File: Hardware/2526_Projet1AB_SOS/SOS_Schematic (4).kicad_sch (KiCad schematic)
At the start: 61 parts, among them J1 USB_C_Receptacle_USB2.0_16P, J2 Conn_ST_STDC14, SW1 SW_SPDT, SW2 SW_Push, SW3 SW_Push, SW4 SW_Push, SW5 SW_Push, U1 BU33SD5WG-TR, U2 USBLC6-2SC6, U3 STM32L476RGTx, Y1 20MHz

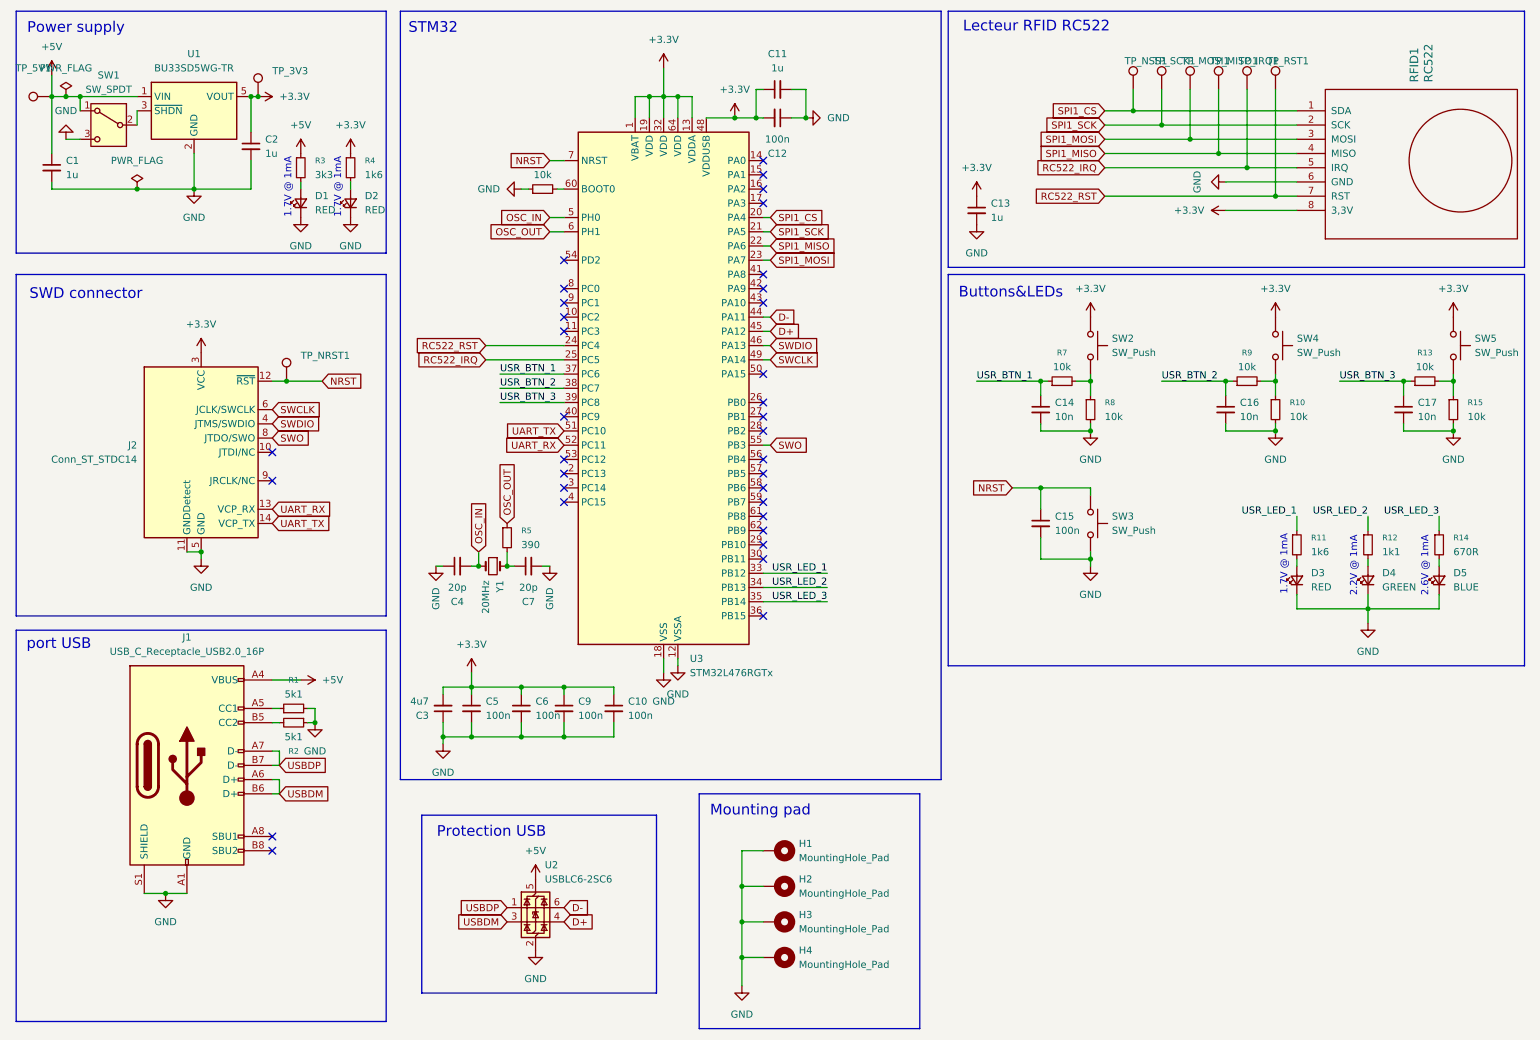
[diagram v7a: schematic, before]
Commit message: Routage Board (sauf port USB)
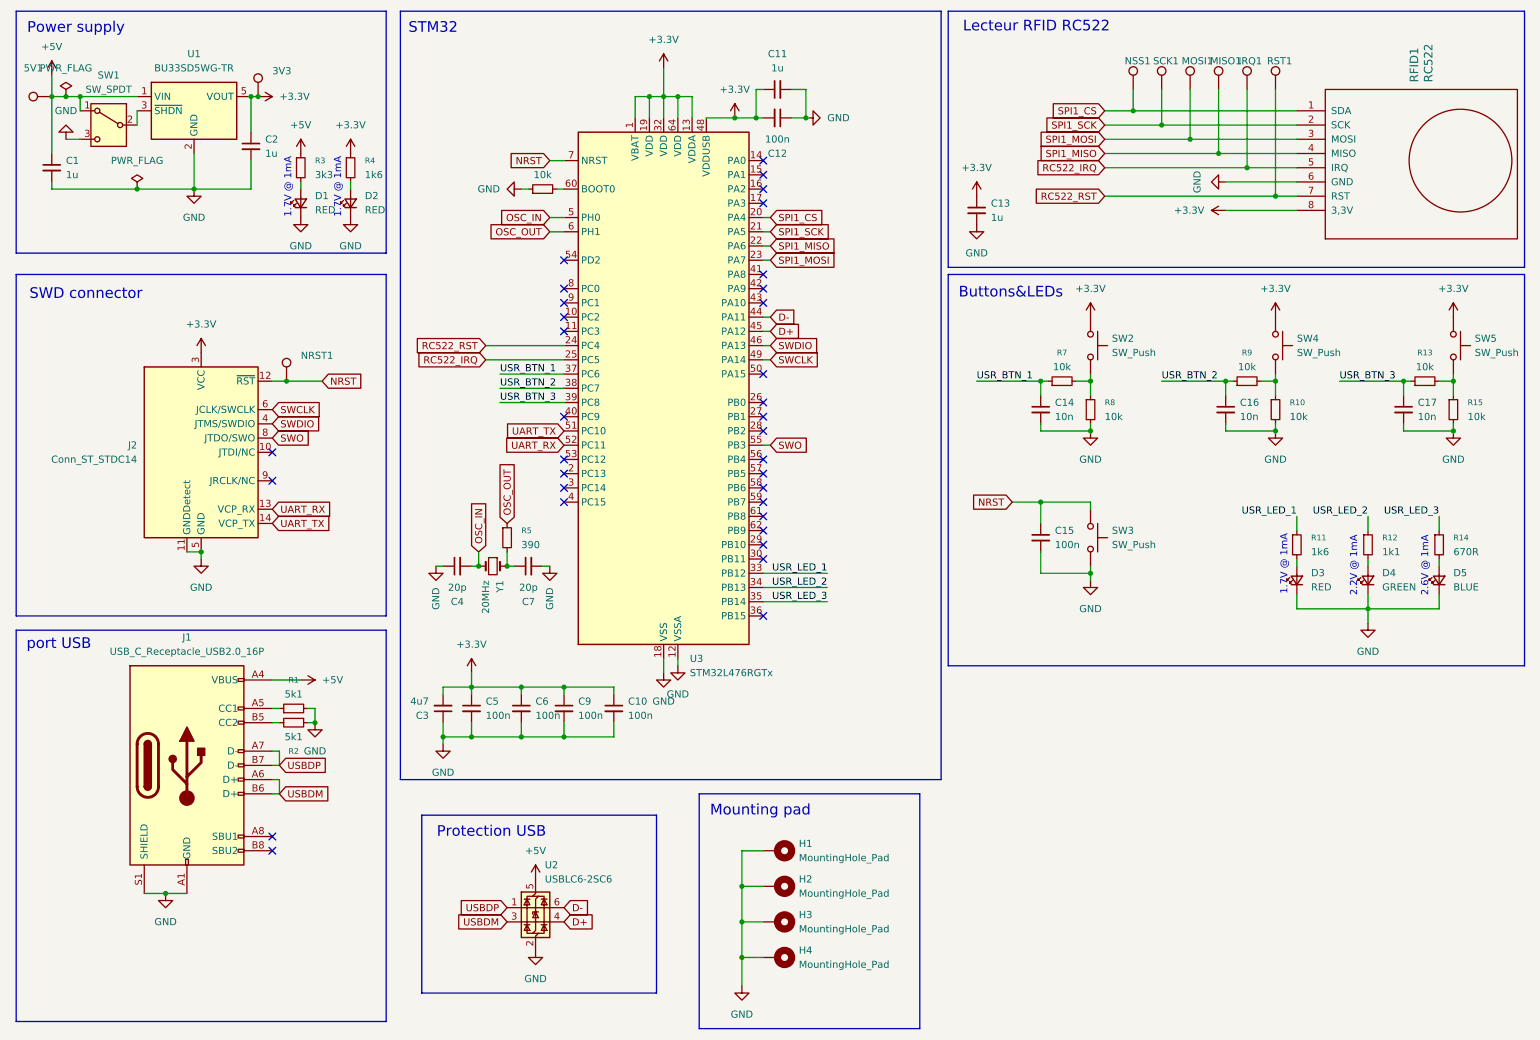
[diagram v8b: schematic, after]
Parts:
- renumbered TP_3V3 to 3V3, TP_5V1 to 5V1, TP_IRQ1 to IRQ1, TP_MISO1 to MISO1, TP_MOSI1 to MOSI1, TP_NRST1 to NRST1, TP_NSS1 to NSS1, TP_RST1 to RST1, TP_SCK1 to SCK1
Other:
- moved on the sheet: C15, SW3
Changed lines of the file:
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@@
 	)
 	(junction
-		(at 196.85 99.06)
+		(at 196.85 101.6)
 		(diameter 0)
 		(color 0 0 0 0)
@@
 	)
 	(junction
-		(at 205.74 111.76)
+		(at 205.74 114.3)
 		(diameter 0)
 		(color 0 0 0 0)
@@
 	(wire
 		(pts
-			(xy 191.77 99.06) (xy 196.85 99.06)
+			(xy 191.77 101.6) (xy 196.85 101.6)
 		)
 		(stroke
@@
 	(wire
 		(pts
-			(xy 196.85 99.06) (xy 196.85 102.87)
+			(xy 196.85 101.6) (xy 196.85 105.41)
 		)
 		(stroke
@@
 	(wire
 		(pts
-			(xy 205.74 111.76) (xy 205.74 113.03)
+			(xy 205.74 114.3) (xy 205.74 115.57)
 		)
 		(stroke
@@
 	(wire
 		(pts
-			(xy 196.85 99.06) (xy 205.74 99.06)
+			(xy 196.85 101.6) (xy 205.74 101.6)
 		)
 		(stroke
@@
 	(wire
 		(pts
-			(xy 196.85 111.76) (xy 205.74 111.76)
+			(xy 196.85 114.3) (xy 205.74 114.3)
 		)
 		(stroke
@@
 	(wire
 		(pts
-			(xy 205.74 99.06) (xy 205.74 100.33)
+			(xy 205.74 101.6) (xy 205.74 102.87)
 		)
 		(stroke
@@
 	(wire
 		(pts
-			(xy 205.74 110.49) (xy 205.74 111.76)
+			(xy 205.74 113.03) (xy 205.74 114.3)
 		)
 		(stroke
@@
 	(wire
 		(pts
-			(xy 196.85 107.95) (xy 196.85 111.76)
+			(xy 196.85 110.49) (xy 196.85 114.3)
 		)
 		(stroke
@@
 	(global_label "NRST"
 		(shape input)
-		(at 191.77 99.06 180)
+		(at 191.77 101.6 180)
 		(fields_autoplaced yes)
 		(effects
@@
 		)
 		(property "Intersheetrefs" "${INTERSHEET_REFS}"
-			(at 184.0072 99.06 0)
+			(at 184.0072 101.6 0)
 			(effects
 				(font
@@
 	(symbol
 		(lib_id "Device:C_Small")
-		(at 196.85 105.41 0)
+		(at 196.85 107.95 0)
 		(unit 1)
 		(exclude_from_sim no)
@@
 		(fields_autoplaced yes)
 		(property "Reference" "C15"
-			(at 199.39 104.1462 0)
+			(at 199.39 106.6862 0)
 			(effects
 				(font
@@
 		)
 		(property "Value" "100n"
-			(at 199.39 106.6862 0)
+			(at 199.39 109.2262 0)
 			(effects
 				(font
@@
 		)
 		(property "Footprint" "Capacitor_SMD:C_0603_1608Metric"
-			(at 196.85 105.41 0)
+			(at 196.85 107.95 0)
 			(effects
 				(font
@@
 		)
 		(property "Datasheet" "~"
-			(at 196.85 105.41 0)
+			(at 196.85 107.95 0)
 			(effects
 				(font
@@
 		)
 		(property "Description" "Unpolarized capacitor, small symbol"
-			(at 196.85 105.41 0)
+			(at 196.85 107.95 0)
 			(effects
 				(font
@@
 		(on_board yes)
 		(dnp no)
-		(property "Reference" "TP_IRQ1"
+		(property "Reference" "IRQ1"
 			(at 232.156 22.86 0)
 			(effects
@@
 			(project "SOS_Schematic (4)"
 				(path "/9d394b3d-e5c0-4919-a596-896a666dc5cf"
-					(reference "TP_IRQ1")
+					(reference "IRQ1")
 					(unit 1)
 				)
@@
 		(on_board yes)
 		(dnp no)
-		(property "Reference" "TP_RST1"
+		(property "Reference" "RST1"
 			(at 237.236 22.86 0)
 			(effects
@@
 			(project "SOS_Schematic (4)"
 				(path "/9d394b3d-e5c0-4919-a596-896a666dc5cf"
-					(reference "TP_RST1")
+					(reference "RST1")
 					(unit 1)
 				)
@@
 		(on_board yes)
 		(dnp no)
-		(property "Reference" "TP_MOSI1"
+		(property "Reference" "MOSI1"
 			(at 221.996 22.86 0)
 			(effects
@@
 			(project "SOS_Schematic (4)"
 				(path "/9d394b3d-e5c0-4919-a596-896a666dc5cf"
-					(reference "TP_MOSI1")
+					(reference "MOSI1")
 					(unit 1)
 				)
@@
 	(symbol
 		(lib_id "Switch:SW_Push")
-		(at 205.74 105.41 270)
+		(at 205.74 107.95 270)
 		(unit 1)
 		(exclude_from_sim no)
@@
 		(fields_autoplaced yes)
 		(property "Reference" "SW3"
-			(at 209.55 104.1399 90)
+			(at 209.55 106.6799 90)
 			(effects
 				(font
@@
 		)
 		(property "Value" "SW_Push"
-			(at 209.55 106.6799 90)
+			(at 209.55 109.2199 90)
 			(effects
 				(font
@@
 		)
 		(property "Footprint" "Button_Switch_SMD:SW_SPST_B3S-1000"
-			(at 210.82 105.41 0)
+			(at 210.82 107.95 0)
 			(effects
 				(font
@@
 		)
 		(property "Datasheet" "~"
-			(at 210.82 105.41 0)
+			(at 210.82 107.95 0)
 			(effects
 				(font
@@
 		)
 		(property "Description" "Push button switch, generic, two pins"
-			(at 205.74 105.41 0)
+			(at 205.74 107.95 0)
 			(effects
 				(font
@@
 		(dnp no)
 		(fields_autoplaced yes)
-		(property "Reference" "TP_3V3"
+		(property "Reference" "3V3"
 			(at 59.69 24.6379 0)
 			(effects
@@
 			(project "SOS_Schematic (4)"
 				(path "/9d394b3d-e5c0-4919-a596-896a666dc5cf"
-					(reference "TP_3V3")
+					(reference "3V3")
 					(unit 1)
 				)
@@
 		(on_board yes)
 		(dnp no)
-		(property "Reference" "TP_SCK1"
+		(property "Reference" "SCK1"
 			(at 216.916 22.86 0)
 			(effects
@@
 			(project "SOS_Schematic (4)"
 				(path "/9d394b3d-e5c0-4919-a596-896a666dc5cf"
-					(reference "TP_SCK1")
+					(reference "SCK1")
 					(unit 1)
 				)
@@
 		(dnp no)
 		(fields_autoplaced yes)
-		(property "Reference" "TP_NRST1"
+		(property "Reference" "NRST1"
 			(at 64.77 75.4379 0)
 			(effects
@@
 			(project "SOS_Schematic (4)"
 				(path "/9d394b3d-e5c0-4919-a596-896a666dc5cf"
-					(reference "TP_NRST1")
+					(reference "NRST1")
 					(unit 1)
 				)
@@
 		(on_board yes)
 		(dnp no)
-		(property "Reference" "TP_NSS1"
+		(property "Reference" "NSS1"
 			(at 211.836 22.86 0)
 			(effects
@@
 			(project "SOS_Schematic (4)"
 				(path "/9d394b3d-e5c0-4919-a596-896a666dc5cf"
-					(reference "TP_NSS1")
+					(reference "NSS1")
 					(unit 1)
 				)
@@
 		(on_board yes)
 		(dnp no)
-		(property "Reference" "TP_MISO1"
+		(property "Reference" "MISO1"
 			(at 227.076 22.86 0)
 			(effects
@@
 			(project "SOS_Schematic (4)"
 				(path "/9d394b3d-e5c0-4919-a596-896a666dc5cf"
-					(reference "TP_MISO1")
+					(reference "MISO1")
 					(unit 1)
 				)
@@
 		(dnp no)
 		(fields_autoplaced yes)
-		(property "Reference" "TP_5V1"
+		(property "Reference" "5V1"
 			(at 17.018 24.13 90)
 			(effects
@@
 			(project ""
 				(path "/9d394b3d-e5c0-4919-a596-896a666dc5cf"
-					(reference "TP_5V1")
+					(reference "5V1")
 					(unit 1)
 				)
@@
 	(symbol
 		(lib_id "power:GND")
-		(at 205.74 113.03 0)
+		(at 205.74 115.57 0)
 		(unit 1)
 		(exclude_from_sim no)
@@
 		(fields_autoplaced yes)
 		(property "Reference" "#PWR032"
-			(at 205.74 119.38 0)
+			(at 205.74 121.92 0)
 			(effects
 				(font
@@
 		)
 		(property "Value" "GND"
-			(at 205.74 118.11 0)
+			(at 205.74 120.65 0)
 			(effects
 				(font
@@
 		)
 		(property "Footprint" ""
-			(at 205.74 113.03 0)
+			(at 205.74 115.57 0)
 			(effects
 				(font
@@
 		)
 		(property "Datasheet" ""
-			(at 205.74 113.03 0)
+			(at 205.74 115.57 0)
 			(effects
 				(font
@@
 		)
 		(property "Description" "Power symbol creates a global label with name \"GND\" , ground"
-			(at 205.74 113.03 0)
+			(at 205.74 115.57 0)
 			(effects
 				(font
